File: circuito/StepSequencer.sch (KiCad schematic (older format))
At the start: 83 parts, among them P1 BEAGLEBONE_BLACK, SW1 SW_PUSH, SW10 SW_PUSH, SW11 SW_PUSH, SW12 SW_PUSH, SW13 SW_PUSH, SW14 SW_PUSH, SW15 SW_PUSH, SW16 SW_PUSH, SW2 SW_PUSH, SW3 SW_PUSH, SW4 SW_PUSH, SW5 SW_PUSH, SW6 SW_PUSH, SW7 SW_PUSH, SW8 SW_PUSH, SW9 SW_PUSH

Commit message: Version para Beagle del Patch.
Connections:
- net btn16 is gone; now on net btn15: P1.A43 (P43), SW16.1
- net led2_16 is gone; now on net led2_15: P1.B30 (P30), R32.2
- net pot2 is gone; now on net pot1: P1.B38 (P38), RV2.2
- net btn1: now also P1.A9 (P9), SW2.1; no longer P1.A7 (P7), SW1.1
- net btn10: now also P1.A33 (P33), SW11.1; no longer P1.A31 (P31), SW10.1
- net btn11: now also P1.A35 (P35), SW12.1; no longer P1.A33 (P33), SW11.1
- net btn12: now also P1.A37 (P37), SW13.1; no longer P1.A35 (P35), SW12.1
- net btn13: now also P1.A39 (P39), SW14.1; no longer P1.A37 (P37), SW13.1
- net btn14: now also P1.A41 (P41), SW15.1; no longer P1.A39 (P39), SW14.1
- net btn15: no longer P1.A41 (P41), SW15.1
- net btn2: now also P1.A11 (P11), SW3.1; no longer P1.A9 (P9), SW2.1
- net btn3: now also P1.A13 (P13), SW4.1; no longer P1.A11 (P11), SW3.1
- net btn4: now also P1.A15 (P15), SW5.1; no longer P1.A13 (P13), SW4.1
- net btn5: now also P1.A17 (P17), SW6.1; no longer P1.A15 (P15), SW5.1
- net btn6: now also P1.A19 (P19), SW7.1; no longer P1.A17 (P17), SW6.1
- net btn7: now also P1.A27 (P27), SW8.1; no longer P1.A19 (P19), SW7.1
- net btn8: now also P1.A29 (P29), SW9.1; no longer P1.A27 (P27), SW8.1
- net btn9: now also P1.A31 (P31), SW10.1; no longer P1.A29 (P29), SW9.1
- net led1_1: now also P1.A10 (P10), R2.2; no longer P1.A8 (P8), R1.2
- net led1_10: now also P1.A34 (P34), R11.2; no longer P1.A32 (P32), R10.2
- net led1_11: now also P1.A36 (P36), R12.2; no longer P1.A34 (P34), R11.2
- net led1_12: now also P1.A38 (P38), R13.2; no longer P1.A36 (P36), R12.2
- net led1_13: now also P1.A40 (P40); no longer P1.A38 (P38), R13.2
- net led1_14: now also P1.A42 (P42); no longer P1.A40 (P40), R14.2
- net led1_15: now also P1.A44 (P44), R14.2; no longer P1.A42 (P42), R15.2
- net led1_16: now also R15.2; no longer P1.A44 (P44), R16.2
- net led1_2: now also P1.A12 (P12), R3.2; no longer P1.A10 (P10), R2.2
- net led1_3: now also P1.A14 (P14), R4.2; no longer P1.A12 (P12), R3.2
- net led1_4: now also P1.A16 (P16), R5.2; no longer P1.A14 (P14), R4.2
- net led1_5: now also P1.A18 (P18), R6.2; no longer P1.A16 (P16), R5.2
- net led1_6: now also P1.A26 (P26); no longer P1.A18 (P18), R6.2
- net led1_7: now also P1.A28 (AP28), R8.2; no longer P1.A26 (P26), R7.2
- net led1_8: now also P1.A30 (P30), R9.2; no longer P1.A28 (AP28), R8.2
- net led1_9: now also P1.A32 (P32), R10.2; no longer P1.A30 (P30), R9.2
- net led2_1: now also P1.B13 (P13), R18.2; no longer P1.B11, R17.2
- net led2_10: now also P1.B16 (P16), R27.2; no longer P1.B14 (P14), R26.2
- net led2_11: now also P1.B18 (P18), R28.2; no longer P1.B16 (P16), R27.2
- net led2_12: now also P1.B22 (P22), R29.2; no longer P1.B18 (P18), R28.2
- net led2_13: now also P1.B24 (P24), R30.2; no longer P1.B22 (P22), R29.2
- net led2_14: now also P1.B26 (P26), R31.2; no longer P1.B24 (P24), R30.2
- net led2_15: no longer P1.B26 (P26), R31.2
- net led2_2: now also P1.B15 (P15), R19.2; no longer P1.B13 (P13), R18.2
- net led2_3: now also P1.B17 (P17), R20.2; no longer P1.B15 (P15), R19.2
- net led2_4: now also P1.B21 (P21), R21.2; no longer P1.B17 (P17), R20.2
- net led2_5: now also P1.B23 (P23), R22.2; no longer P1.B21 (P21), R21.2
- net led2_6: now also P1.B27 (P27), R23.2; no longer P1.B23 (P23), R22.2
- net led2_7: now also P1.B41 (P41), R24.2; no longer P1.B27 (P27), R23.2
- net led2_8: now also P1.B12 (P12), R25.2; no longer P1.B41 (P41), R24.2
- net led2_9: now also P1.B14 (P14), R26.2; no longer P1.B12 (P12), R25.2
- net pot1: no longer P1.B40 (P40), RV1.2
- new net btn0: P1.A7 (P7), SW1.1
- new net led1_0: P1.A8 (P8), R1.2
- new net led1_17: R16.2
- new net led1_6.: R7.2
- new net led2_0: P1.B11, R17.2
- new net pot0: P1.B40 (P40), RV1.2
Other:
- note added: "Leds Onset"
- note added: "Leds Tiempo"
- moved on the sheet: D1, D10, D11, D12, D13, D14, D15, D16, D17, D18, D19, D2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

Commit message: Empezando layout del pcb
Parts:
- RV1, RV2: footprint Potentiometers:Potentiometer_Alps-RK163-single_20mm -> StepSequencer:POT_AZUL
- renumbered D1 to D1_0, D2 to D1_1, D11 to D1_10, D12 to D1_11, D13 to D1_12, D14 to D1_13, D15 to D1_14, D16 to D1_15, D3 to D1_2, D4 to D1_3, D5 to D1_4, D6 to D1_5, D7 to D1_6, D8 to D1_7, D9 to D1_8, D10 to D1_9, D17 to D2_0, D18 to D2_1, D27 to D2_10, D28 to D2_11, D29 to D2_12, D30 to D2_13, D31 to D2_14, D32 to D2_15, D19 to D2_2, D20 to D2_3, D21 to D2_4, D22 to D2_5, D23 to D2_6, D24 to D2_7, D25 to D2_8, D26 to D2_9, R1 to R1_0, R2 to R1_1, R11 to R1_10, R12 to R1_11, R13 to R1_12, R14 to R1_13, R15 to R1_14, R16 to R1_15, R3 to R1_2, R4 to R1_3, R5 to R1_4, R6 to R1_5, R7 to R1_6, R8 to R1_7, R9 to R1_8, R10 to R1_9, R17 to R2_0, R18 to R2_1, R27 to R2_10, R28 to R2_11, R29 to R2_12, R30 to R2_13, R31 to R2_14, R32 to R2_15, R19 to R2_2, R20 to R2_3, R21 to R2_4, R22 to R2_5, R23 to R2_6, R24 to R2_7, R25 to R2_8, R26 to R2_9, SW1 to SW0, SW2 to SW1, SW11 to SW10, SW12 to SW11, SW13 to SW12, SW14 to SW13, SW15 to SW14, SW16 to SW15, SW3 to SW2, SW4 to SW3, SW5 to SW4, SW6 to SW5, SW7 to SW6, SW8 to SW7, SW9 to SW8, SW10 to SW9
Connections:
- net led1_16 is gone; now on net led1_14: R1_14.2
- net led1_17 is gone; now on net led1_15: R1_15.2
- net led1_13: now also R1_13.2
- net led1_15: no longer R1_13.2

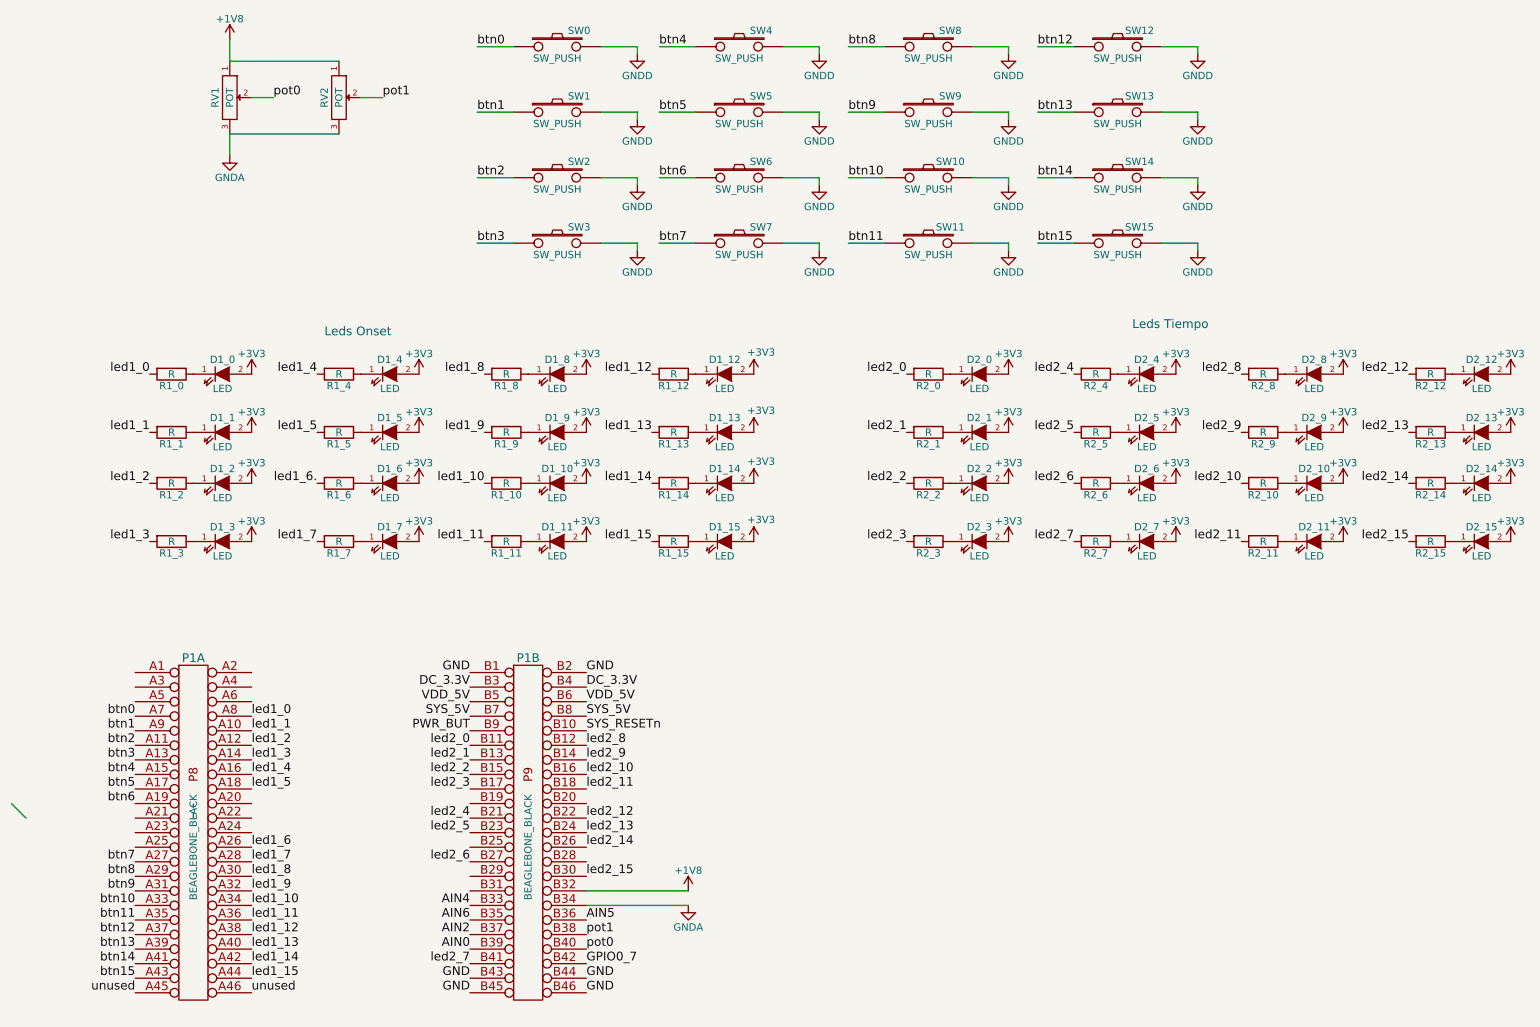
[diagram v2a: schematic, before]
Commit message: PBC ruteado de leds, botones, beagle, faltan pots y tierras.
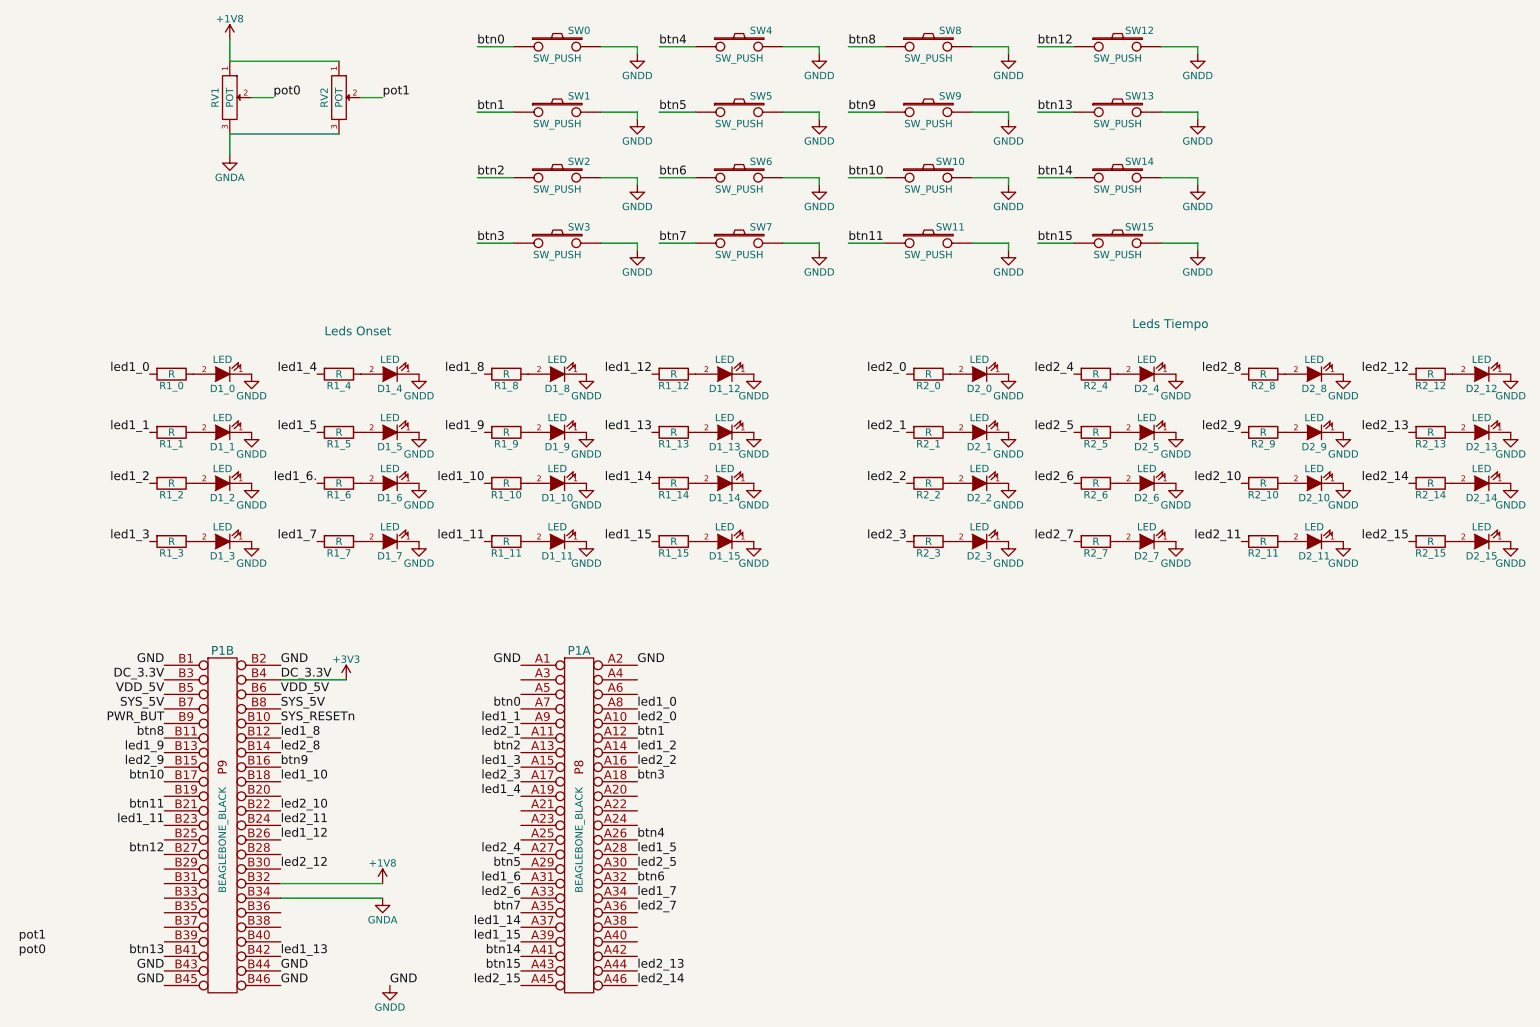
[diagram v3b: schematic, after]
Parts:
- P1: footprint beagleboard:BEAGLEBONE_BLACK -> StepSequencer:BEAGLEBONE_BLACK
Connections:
- net DC_3.3V is gone; now on net +3V3: P1.B3, P1.B4 (P4)
- net GND is gone; now on net GNDD: P1.B1 (GND), P1.B2 (P2), P1.B43 (P43), P1.B44 (P44), P1.B45 (P45), P1.B46 (P46)
- net GPIO0_7 is gone; now on net led1_13: P1.B42 (P42)
- net +3V3: no longer D1_0.2 (A), D1_1.2 (A), D1_10.2 (A), D1_11.2 (A), D1_12.2 (A), D1_13.2 (A), D1_14.2 (A), D1_15.2 (A), D1_2.2 (A), D1_3.2 (A), D1_4.2 (A), D1_5.2 (A), D1_6.2 (A), D1_7.2 (A), D1_8.2 (A), D1_9.2 (A), D2_0.2 (A), D2_1.2 (A), D2_10.2 (A), D2_11.2 (A), D2_12.2 (A), D2_13.2 (A), D2_14.2 (A), D2_15.2 (A), D2_2.2 (A), D2_3.2 (A), D2_4.2 (A), D2_5.2 (A), D2_6.2 (A), D2_7.2 (A), D2_8.2 (A), D2_9.2 (A)
- net GNDD: now also D1_0.1 (K), D1_1.1 (K), D1_10.1 (K), D1_11.1 (K), D1_12.1 (K), D1_13.1 (K), D1_14.1 (K), D1_15.1 (K), D1_2.1 (K), D1_3.1 (K), D1_4.1 (K), D1_5.1 (K), D1_6.1 (K), D1_7.1 (K), D1_8.1 (K), D1_9.1 (K), D2_0.1 (K), D2_1.1 (K), D2_10.1 (K), D2_11.1 (K), D2_12.1 (K), D2_13.1 (K), D2_14.1 (K), D2_15.1 (K), D2_2.1 (K), D2_3.1 (K), D2_4.1 (K), D2_5.1 (K), D2_6.1 (K), D2_7.1 (K), D2_8.1 (K), D2_9.1 (K), P1.A1 (GND), P1.A2 (P2)
- net btn1: now also P1.A12 (P12); no longer P1.A9 (P9)
- net btn10: now also P1.B17 (P17); no longer P1.A33 (P33)
- net btn11: now also P1.B21 (P21); no longer P1.A35 (P35)
- net btn12: now also P1.B27 (P27); no longer P1.A37 (P37)
- net btn13: now also P1.B41 (P41); no longer P1.A39 (P39)
- net btn2: now also P1.A13 (P13); no longer P1.A11 (P11)
- net btn3: now also P1.A18 (P18); no longer P1.A13 (P13)
- net btn4: now also P1.A26 (P26); no longer P1.A15 (P15)
- net btn5: now also P1.A29 (P29); no longer P1.A17 (P17)
- net btn6: now also P1.A32 (P32); no longer P1.A19 (P19)
- net btn7: now also P1.A35 (P35); no longer P1.A27 (P27)
- net btn8: now also P1.B11; no longer P1.A29 (P29)
- net btn9: now also P1.B16 (P16); no longer P1.A31 (P31)
- net led1_1: now also P1.A9 (P9); no longer P1.A10 (P10)
- net led1_10: now also P1.B18 (P18); no longer P1.A34 (P34)
- net led1_11: now also P1.B23 (P23); no longer P1.A36 (P36)
- net led1_12: now also P1.B26 (P26); no longer P1.A38 (P38)
- net led1_13: no longer P1.A40 (P40)
- net led1_14: now also P1.A37 (P37); no longer P1.A42 (P42)
- net led1_15: now also P1.A39 (P39); no longer P1.A44 (P44)
- net led1_2: now also P1.A14 (P14); no longer P1.A12 (P12)
- net led1_3: now also P1.A15 (P15); no longer P1.A14 (P14)
- net led1_4: now also P1.A19 (P19); no longer P1.A16 (P16)
- net led1_5: now also P1.A28 (AP28); no longer P1.A18 (P18)
- net led1_6: now also P1.A31 (P31); no longer P1.A26 (P26)
- net led1_7: now also P1.A34 (P34); no longer P1.A28 (AP28)
- net led1_8: now also P1.B12 (P12); no longer P1.A30 (P30)
- net led1_9: now also P1.B13 (P13); no longer P1.A32 (P32)
- net led2_0: now also P1.A10 (P10); no longer P1.B11
- net led2_1: now also P1.A11 (P11); no longer P1.B13 (P13)
- net led2_10: now also P1.B22 (P22); no longer P1.B16 (P16)
- net led2_11: now also P1.B24 (P24); no longer P1.B18 (P18)
- net led2_12: now also P1.B30 (P30); no longer P1.B22 (P22)
- net led2_13: now also P1.A44 (P44); no longer P1.B24 (P24)
- net led2_14: now also P1.A46 (P46); no longer P1.B26 (P26)
- net led2_15: now also P1.A45 (P45); no longer P1.B30 (P30)
- net led2_2: now also P1.A16 (P16); no longer P1.B15 (P15)
- net led2_3: now also P1.A17 (P17); no longer P1.B17 (P17)
- net led2_4: now also P1.A27 (P27); no longer P1.B21 (P21)
- net led2_5: now also P1.A30 (P30); no longer P1.B23 (P23)
- net led2_6: now also P1.A33 (P33); no longer P1.B27 (P27)
- net led2_7: now also P1.A36 (P36); no longer P1.B41 (P41)
- net led2_8: now also P1.B14 (P14); no longer P1.B12 (P12)
- net led2_9: now also P1.B15 (P15); no longer P1.B14 (P14)
- net pot0: no longer P1.B40 (P40)
- net pot1: no longer P1.B38 (P38)
- net at R1_9.1: now also D1_9.2 (A); no longer D1_9.1 (K)
- net at R1_8.1: now also D1_8.2 (A); no longer D1_8.1 (K)
- net at R1_11.1: now also D1_11.2 (A); no longer D1_11.1 (K)
- net at R1_10.1: now also D1_10.2 (A); no longer D1_10.1 (K)
- net at R1_13.1: now also D1_13.2 (A); no longer D1_13.1 (K)
- net at R1_12.1: now also D1_12.2 (A); no longer D1_12.1 (K)
- net at R1_15.1: now also D1_15.2 (A); no longer D1_15.1 (K)
- net at R1_14.1: now also D1_14.2 (A); no longer D1_14.1 (K)
- net at R1_1.1: now also D1_1.2 (A); no longer D1_1.1 (K)
- net at R1_0.1: now also D1_0.2 (A); no longer D1_0.1 (K)
- net at R1_3.1: now also D1_3.2 (A); no longer D1_3.1 (K)
- net at R1_2.1: now also D1_2.2 (A); no longer D1_2.1 (K)
- net at R1_5.1: now also D1_5.2 (A); no longer D1_5.1 (K)
- net at R1_4.1: now also D1_4.2 (A); no longer D1_4.1 (K)
- net at R1_7.1: now also D1_7.2 (A); no longer D1_7.1 (K)
- net at R1_6.1: now also D1_6.2 (A); no longer D1_6.1 (K)
- net at R2_9.1: now also D2_9.2 (A); no longer D2_9.1 (K)
- net at R2_8.1: now also D2_8.2 (A); no longer D2_8.1 (K)
- net at R2_11.1: now also D2_11.2 (A); no longer D2_11.1 (K)
- net at R2_10.1: now also D2_10.2 (A); no longer D2_10.1 (K)
- net at R2_13.1: now also D2_13.2 (A); no longer D2_13.1 (K)
- net at R2_12.1: now also D2_12.2 (A); no longer D2_12.1 (K)
- net at R2_15.1: now also D2_15.2 (A); no longer D2_15.1 (K)
- net at R2_14.1: now also D2_14.2 (A); no longer D2_14.1 (K)
- net at R2_1.1: now also D2_1.2 (A); no longer D2_1.1 (K)
- net at R2_0.1: now also D2_0.2 (A); no longer D2_0.1 (K)
- net at R2_3.1: now also D2_3.2 (A); no longer D2_3.1 (K)
- net at R2_2.1: now also D2_2.2 (A); no longer D2_2.1 (K)
- net at R2_5.1: now also D2_5.2 (A); no longer D2_5.1 (K)
- net at R2_4.1: now also D2_4.2 (A); no longer D2_4.1 (K)
- net at R2_7.1: now also D2_7.2 (A); no longer D2_7.1 (K)
- net at R2_6.1: now also D2_6.2 (A); no longer D2_6.1 (K)
- net AIN0: no longer names the net of P1.B39 (P39)
- net AIN2: no longer names the net of P1.B37 (P37)
- net AIN4: no longer names the net of P1.B33 (P33)
- net AIN5: no longer names the net of P1.B36 (P36)
- net AIN6: no longer names the net of P1.B35 (P35)
- removed net unused: P1.A45 (P45), P1.A46 (P46)
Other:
- moved on the sheet: P1A, P1B

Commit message: PCB Casi listo
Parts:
- D1_0, D1_1, D1_10, D1_11, D1_12, D1_13, D1_14, D1_15, D1_2, D1_3, D1_4, D1_5, D1_6, D1_7, D1_8, D1_9, D2_0, D2_1, D2_10, D2_11, D2_12, D2_13, D2_14, D2_15, D2_2, D2_3, D2_4, D2_5, D2_6, D2_7, D2_8, D2_9: footprint LEDs:LED-5MM -> LEDs:LED-3MM
- SW0, SW1, SW10, SW11, SW12, SW13, SW14, SW15, SW2, SW3, SW4, SW5, SW6, SW7, SW8, SW9: footprint Buttons_Switches_ThroughHole:SW_PUSH-12mm -> StepSequencer:BOTON
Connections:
- net +1V8: now also RV1.3, RV2.3; no longer RV1.1, RV2.1
- net GNDD: now also P1.B34 (P34), RV1.1, RV2.1
- net pot0: now also P1.B37 (P37)
- net pot1: now also P1.B39 (P39)
- removed net GNDA: P1.B34 (P34), RV1.3, RV2.3
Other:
- moved on the sheet: RV1, RV2

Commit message: Gato, gerber
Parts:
- added P2, P3, P4, P5: CONN_01X01, StepSequencer:SCREWS, symbol CONN_01X01
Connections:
- net GNDD: now also P2.1 (P1), P3.1 (P1), P4.1 (P1), P5.1 (P1)
